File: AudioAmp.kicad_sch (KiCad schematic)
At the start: 56 parts, among them J1 ACJS-MHOM, J2 ACJS-MHOM, Q1 MJE182G, Q12 MMBT5401, Q13 MMBT5401, Q2 MJE172G, Q3 MMBT5551(RANGE:200-300), Q9 MMBT5551(RANGE:200-300)

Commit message: change: Testpoints
Testpoint footprints
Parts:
- TP1, TP10, TP2, TP3, TP5, TP7, TP8, TP9: footprint (none) -> TestPoint:TestPoint_Pad_1.0x1.0mm
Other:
- company: Lucca, Marcel -> Lucca Kuvecke, Marcel Tanneberger
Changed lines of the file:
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@@
 	(title_block
 		(title "Audio Amp")
-		(date "2025-04-20")
-		(rev "1")
-		(company "Lucca, Marcel")
+		(date "2025-04-29")
+		(rev "1.1")
+		(company "Lucca Kuvecke, Marcel Tanneberger")
 	)
 	(text "Testpoints brauchen keinen Footprint."
@@
 			)
 		)
-		(property "Footprint" ""
+		(property "Footprint" "TestPoint:TestPoint_Pad_1.0x1.0mm"
 			(at 130.81 77.47 0)
 			(effects
@@
 			)
 		)
-		(property "Footprint" ""
+		(property "Footprint" "TestPoint:TestPoint_Pad_1.0x1.0mm"
 			(at 137.16 138.43 0)
 			(effects
@@
 			)
 		)
-		(property "Footprint" ""
+		(property "Footprint" "TestPoint:TestPoint_Pad_1.0x1.0mm"
 			(at 137.16 128.27 0)
 			(effects
@@
 			)
 		)
-		(property "Footprint" ""
+		(property "Footprint" "TestPoint:TestPoint_Pad_1.0x1.0mm"
 			(at 212.09 73.66 0)
 			(effects
@@
 			)
 		)
-		(property "Footprint" ""
+		(property "Footprint" "TestPoint:TestPoint_Pad_1.0x1.0mm"
 			(at 99.06 77.47 0)
 			(effects
@@
 			)
 		)
-		(property "Footprint" ""
+		(property "Footprint" "TestPoint:TestPoint_Pad_1.0x1.0mm"
 			(at 138.43 111.76 0)
 			(effects
@@
 			)
 		)
-		(property "Footprint" ""
+		(property "Footprint" "TestPoint:TestPoint_Pad_1.0x1.0mm"
 			(at 116.84 50.8 0)
 			(effects
@@
 			)
 		)
-		(property "Footprint" ""
+		(property "Footprint" "TestPoint:TestPoint_Pad_1.0x1.0mm"
 			(at 171.45 86.36 0)
 			(effects

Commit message: ignores hingefügt
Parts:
- TP4: footprint (none) -> TestPoint:TestPoint_Pad_1.0x1.0mm
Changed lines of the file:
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@@
 			)
 		)
-		(property "Footprint" ""
+		(property "Footprint" "TestPoint:TestPoint_Pad_1.0x1.0mm"
 			(at 210.82 100.33 0)
 			(effects

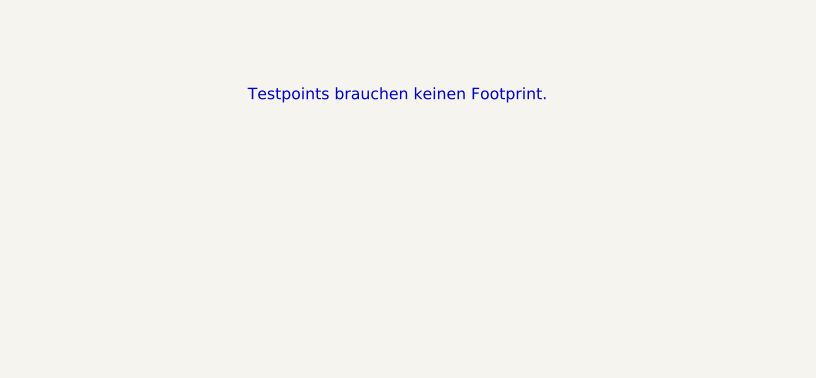
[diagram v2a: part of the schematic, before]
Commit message: CHA: Footprint von Pin auf Fläche
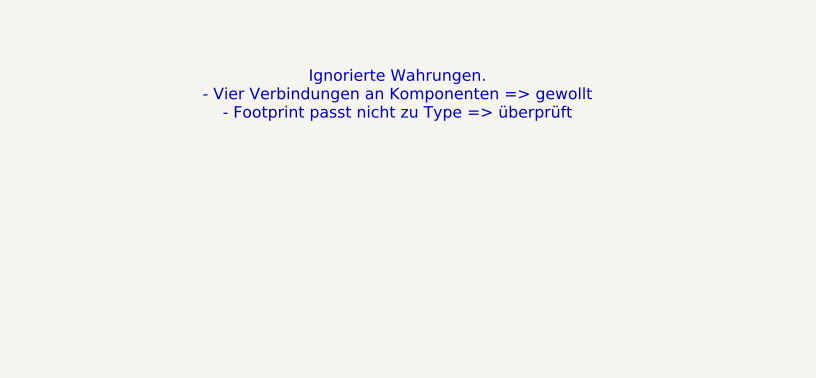
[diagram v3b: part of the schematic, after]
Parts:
- TP1, TP10, TP2, TP3, TP4, TP5, TP7, TP8, TP9: footprint TestPoint:TestPoint_Pad_1.0x1.0mm -> Connector_Pin:Pin_D1.0mm_L10.0mm
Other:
- note added: "Ignorierte Wahrungen. - Vier Verbindungen an Komponenten => gewollt - Footprint passt nicht zu Type => überprüft"
- note removed: "Testpoints brauchen keinen Footprint."
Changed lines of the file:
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@@
 		(company "Lucca Kuvecke, Marcel Tanneberger")
 	)
-	(text "Testpoints brauchen keinen Footprint."
+	(text "Ignorierte Wahrungen. \n- Vier Verbindungen an Komponenten => gewollt\n- Footprint passt nicht zu Type => überprüft\n"
 		(exclude_from_sim no)
 		(at 53.848 40.64 0)
@@
 			)
 		)
-		(property "Footprint" "TestPoint:TestPoint_Pad_1.0x1.0mm"
+		(property "Footprint" "Connector_Pin:Pin_D1.0mm_L10.0mm"
 			(at 130.81 77.47 0)
 			(effects
@@
 			)
 		)
-		(property "Footprint" "TestPoint:TestPoint_Pad_1.0x1.0mm"
+		(property "Footprint" "Connector_Pin:Pin_D1.0mm_L10.0mm"
 			(at 137.16 138.43 0)
 			(effects
@@
 			)
 		)
-		(property "Footprint" "TestPoint:TestPoint_Pad_1.0x1.0mm"
+		(property "Footprint" "Connector_Pin:Pin_D1.0mm_L10.0mm"
 			(at 137.16 128.27 0)
 			(effects
@@
 			)
 		)
-		(property "Footprint" "TestPoint:TestPoint_Pad_1.0x1.0mm"
+		(property "Footprint" "Connector_Pin:Pin_D1.0mm_L10.0mm"
 			(at 212.09 73.66 0)
 			(effects
@@
 			)
 		)
-		(property "Footprint" "TestPoint:TestPoint_Pad_1.0x1.0mm"
+		(property "Footprint" "Connector_Pin:Pin_D1.0mm_L10.0mm"
 			(at 99.06 77.47 0)
 			(effects
@@
 			)
 		)
-		(property "Footprint" "TestPoint:TestPoint_Pad_1.0x1.0mm"
+		(property "Footprint" "Connector_Pin:Pin_D1.0mm_L10.0mm"
 			(at 138.43 111.76 0)
 			(effects
@@
 			)
 		)
-		(property "Footprint" "TestPoint:TestPoint_Pad_1.0x1.0mm"
+		(property "Footprint" "Connector_Pin:Pin_D1.0mm_L10.0mm"
 			(at 116.84 50.8 0)
 			(effects
@@
 			)
 		)
-		(property "Footprint" "TestPoint:TestPoint_Pad_1.0x1.0mm"
+		(property "Footprint" "Connector_Pin:Pin_D1.0mm_L10.0mm"
 			(at 171.45 86.36 0)
 			(effects
@@
 			)
 		)
-		(property "Footprint" "TestPoint:TestPoint_Pad_1.0x1.0mm"
+		(property "Footprint" "Connector_Pin:Pin_D1.0mm_L10.0mm"
 			(at 210.82 100.33 0)
 			(effects
